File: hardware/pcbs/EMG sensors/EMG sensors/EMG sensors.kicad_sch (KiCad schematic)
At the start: 28 parts, among them IC1 INA128, U6 OPA2188AIDR, U7 OPA188AIDR

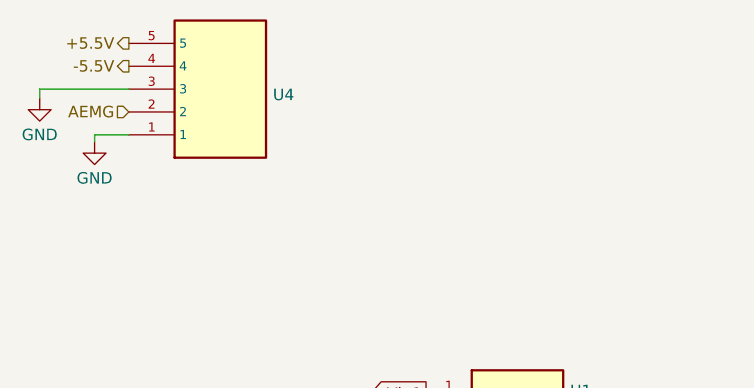
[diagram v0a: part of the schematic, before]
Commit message: Voltage supply of sEMG & ADC
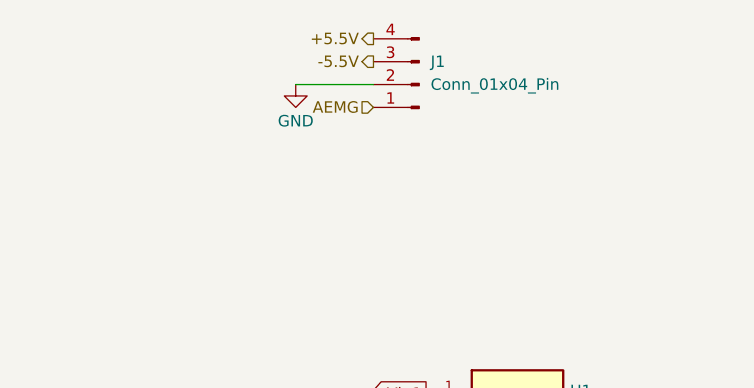
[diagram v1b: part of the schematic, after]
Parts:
- removed U4: ~, Connector_JST:JST_GH_BM05B-GHS-TBT_1x05-1MP_P1.25mm_Vertical, symbol headers:H_5
- added J1: Conn_01x04_Pin, Connector_JST:JST_GH_BM04B-GHS-TBT_1x04-1MP_P1.25mm_Vertical, symbol Connector:Conn_01x04_Pin
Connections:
- net +5.5V: now also J1.4 (Pin_4)
- net -5.5V: now also J1.3 (Pin_3)
- net AEMG: now also J1.1 (Pin_1)
- net GND: now also J1.2 (Pin_2)
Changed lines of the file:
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@@
 (kicad_sch
-	(version 20231120)
+	(version 20250114)
 	(generator "eeschema")
-	(generator_version "8.0")
+	(generator_version "9.0")
 	(paper "A4")
 	(junction
@@
 	(wire
 		(pts
+			(xy 54.61 29.21) (xy 63.246 29.21)
+		)
+		(stroke
+			(width 0)
+			(type default)
+		)
+	)
+	(wire
+		(pts
 			(xy 51.054 102.108) (xy 51.054 103.378)
 		)
@@
 	(wire
 		(pts
-			(xy 36.068 34.798) (xy 32.258 34.798)
-		)
-		(stroke
-			(width 0)
-			(type default)
-		)
-	)
-	(wire
-		(pts
 			(xy 240.284 75.184) (xy 249.936 75.184)
 		)
@@
 	(wire
 		(pts
-			(xy 32.258 34.798) (xy 32.258 35.56)
-		)
-		(stroke
-			(width 0)
-			(type default)
-		)
-	)
-	(wire
-		(pts
 			(xy 249.936 76.962) (xy 249.936 75.184)
 		)
@@
 	(wire
 		(pts
-			(xy 26.162 29.718) (xy 36.068 29.718)
-		)
-		(stroke
-			(width 0)
-			(type default)
-		)
-	)
-	(wire
-		(pts
 			(xy 156.21 86.36) (xy 140.716 86.36)
 		)
@@
 	(wire
 		(pts
-			(xy 26.162 29.718) (xy 26.162 30.734)
-		)
-		(stroke
-			(width 0)
-			(type default)
-		)
-	)
-	(wire
-		(pts
 			(xy 132.842 114.808) (xy 132.842 139.7)
 		)
@@
 		)
 	)
-	(hierarchical_label "+5.5V"
-		(shape output)
-		(at 36.068 24.638 180)
-		(effects
-			(font
-				(size 1.27 1.27)
-			)
-			(justify right)
-		)
-	)
 	(hierarchical_label "-5.5V"
 		(shape input)
@@
 		)
 	)
-	(hierarchical_label "-5.5V"
-		(shape output)
-		(at 36.068 27.178 180)
-		(effects
-			(font
-				(size 1.27 1.27)
-			)
-			(justify right)
-		)
-	)
 	(hierarchical_label "+5.5V"
 		(shape input)
@@
 		)
 	)
-	(hierarchical_label "AEMG"
-		(shape input)
-		(at 36.068 32.258 180)
+	(hierarchical_label "-5.5V"
+		(shape output)
+		(at 63.246 26.67 180)
 		(effects
 			(font
@@
 		)
 	)
+	(hierarchical_label "AEMG"
+		(shape input)
+		(at 63.246 31.75 180)
+		(effects
+			(font
+				(size 1.27 1.27)
+			)
+			(justify right)
+		)
+	)
 	(hierarchical_label "-5.5V"
 		(shape input)
@@
 		)
 	)
+	(hierarchical_label "+5.5V"
+		(shape output)
+		(at 63.246 24.13 180)
+		(effects
+			(font
+				(size 1.27 1.27)
+			)
+			(justify right)
+		)
+	)
 	(hierarchical_label "-5.5V"
 		(shape input)
@@
 	(symbol
 		(lib_id "power:GND")
-		(at 26.162 30.734 0)
+		(at 54.61 29.21 0)
 		(unit 1)
 		(exclude_from_sim no)
@@
 		(dnp no)
 		(property "Reference" "#PWR04"
-			(at 26.162 37.084 0)
+			(at 54.61 35.56 0)
 			(effects
 				(font
@@
 		)
 		(property "Value" "GND"
-			(at 26.162 34.798 0)
+			(at 54.61 33.274 0)
 			(effects
 				(font
@@
 		)
 		(property "Footprint" ""
-			(at 26.162 30.734 0)
+			(at 54.61 29.21 0)
 			(effects
 				(font
@@
 		)
 		(property "Datasheet" ""
-			(at 26.162 30.734 0)
+			(at 54.61 29.21 0)
 			(effects
 				(font
@@
 		)
 		(property "Description" "Power symbol creates a global label with name \"GND\" , ground"
-			(at 26.162 30.734 0)
+			(at 54.61 29.21 0)
 			(effects
 				(font
@@
 	)
 	(symbol
-		(lib_id "headers:H_5")
-		(at 32.258 28.448 0)
-		(mirror x)
-		(unit 1)
-		(exclude_from_sim no)
-		(in_bom yes)
-		(on_board yes)
-		(dnp no)
-		(property "Reference" "U4"
-			(at 52.07 30.3531 0)
-			(effects
-				(font
-					(size 1.27 1.27)
-				)
-				(justify left)
-			)
-		)
-		(property "Value" "~"
-			(at 52.07 28.448 0)
-			(effects
-				(font
-					(size 1.27 1.27)
-				)
-				(justify left)
-			)
-		)
-		(property "Footprint" "Connector_JST:JST_GH_BM05B-GHS-TBT_1x05-1MP_P1.25mm_Vertical"
-			(at 32.258 28.448 0)
-			(effects
-				(font
-					(size 1.27 1.27)
-				)
-				(hide yes)
-			)
-		)
-		(property "Datasheet" ""
-			(at 32.258 28.448 0)
-			(effects
-				(font
-					(size 1.27 1.27)
-				)
-				(hide yes)
-			)
-		)
-		(property "Description" ""
-			(at 32.258 28.448 0)
-			(effects
-				(font
-					(size 1.27 1.27)
-				)
-				(hide yes)
-			)
-		)
-		(pin "3"
-		)
-		(pin "2"
-		)
-		(pin "1"
-		)
-		(pin "5"
-		)
-		(pin "4"
-		)
-		(instances
-			(project "EMG sensors"
-				(path "/a1d73765-1778-424a-b5d5-45dcc9997ebd"
-					(reference "U4")
-					(unit 1)
-				)
-			)
-		)
-	)
-	(symbol
 		(lib_id "Device:R")
 		(at 103.378 102.108 90)
@@
 	)
 	(symbol
+		(lib_id "Connector:Conn_01x04_Pin")
+		(at 68.326 29.21 180)
+		(unit 1)
+		(exclude_from_sim no)
+		(in_bom yes)
+		(on_board yes)
+		(dnp no)
+		(fields_autoplaced yes)
+		(property "Reference" "J1"
+			(at 69.596 26.6699 0)
+			(effects
+				(font
+					(size 1.27 1.27)
+				)
+				(justify right)
+			)
+		)
+		(property "Value" "Conn_01x04_Pin"
+			(at 69.596 29.2099 0)
+			(effects
+				(font
+					(size 1.27 1.27)
+				)
+				(justify right)
+			)
+		)
+		(property "Footprint" "Connector_JST:JST_GH_BM04B-GHS-TBT_1x04-1MP_P1.25mm_Vertical"
+			(at 68.326 29.21 0)
+			(effects
+				(font
+					(size 1.27 1.27)
+				)
+				(hide yes)
+			)
+		)
+		(property "Datasheet" "~"
+			(at 68.326 29.21 0)
+			(effects
+				(font
+					(size 1.27 1.27)
+				)
+				(hide yes)
+			)
+		)
+		(property "Description" "Generic connector, single row, 01x04, script generated"
+			(at 68.326 29.21 0)
+			(effects
+				(font
+					(size 1.27 1.27)
+				)
+				(hide yes)
+			)
+		)
+		(pin "2"
+		)
+		(pin "3"
+		)
+		(pin "1"
+		)
+		(pin "4"
+		)
+		(instances
+			(project ""
+				(path "/a1d73765-1778-424a-b5d5-45dcc9997ebd"
+					(reference "J1")
+					(unit 1)
+				)
+			)
+		)
+	)
+	(symbol
 		(lib_id "Device:R")
 		(at 165.608 131.826 270)
@@
 	)
 	(symbol
-		(lib_id "power:GND")
-		(at 32.258 35.56 0)
-		(unit 1)
-		(exclude_from_sim no)
-		(in_bom yes)
-		(on_board yes)
-		(dnp no)
-		(property "Reference" "#PWR05"
-			(at 32.258 41.91 0)
-			(effects
-				(font
-					(size 1.27 1.27)
-				)
-				(hide yes)
-			)
-		)
-		(property "Value" "GND"
-			(at 32.258 39.624 0)
-			(effects
-				(font
-					(size 1.27 1.27)
-				)
-			)
-		)
-		(property "Footprint" ""
-			(at 32.258 35.56 0)
-			(effects
-				(font
-					(size 1.27 1.27)
-				)
-				(hide yes)
-			)
-		)
-		(property "Datasheet" ""
-			(at 32.258 35.56 0)
-			(effects
-				(font
-					(size 1.27 1.27)
-				)
-				(hide yes)
-			)
-		)
-		(property "Description" "Power symbol creates a global label with name \"GND\" , ground"
-			(at 32.258 35.56 0)
-			(effects
-				(font
-					(size 1.27 1.27)
-				)
-				(hide yes)
-			)
-		)
-		(pin "1"
-		)
-		(instances
-			(project "EMG sensors"
-				(path "/a1d73765-1778-424a-b5d5-45dcc9997ebd"
-					(reference "#PWR05")
-					(unit 1)
-				)
-			)
-		)
-	)
-	(symbol
 		(lib_id "Device:C")
 		(at 194.056 80.772 0)
@@
 		)
 	)
+	(embedded_fonts no)
 )
